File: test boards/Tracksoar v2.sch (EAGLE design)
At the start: 37 parts, among them IC1 BME280, IC2 74AHC1G125DBV, Y1 16MHZ

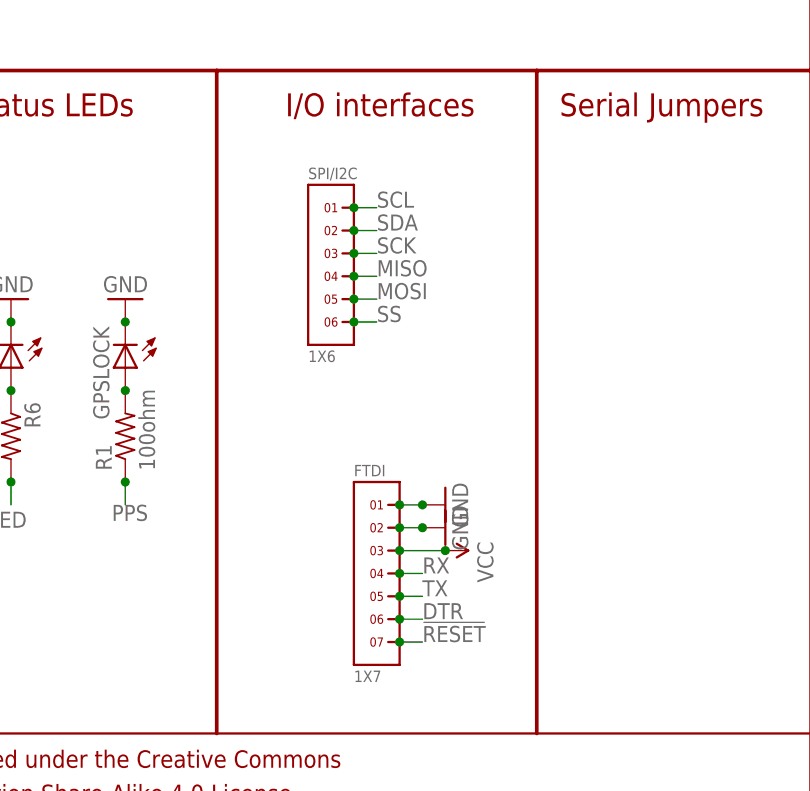
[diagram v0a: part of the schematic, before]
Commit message: Removed v1.1 headers
removed the v1.1 headers to simplify layout.
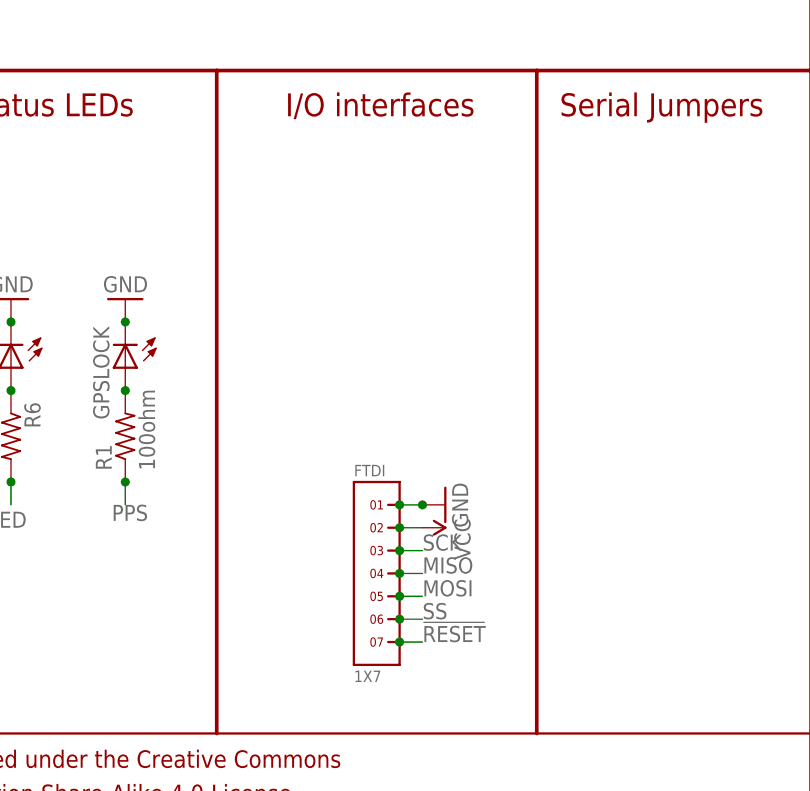
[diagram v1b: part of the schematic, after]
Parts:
- removed SPI/I2C: 1X6, headers(2mm):1X6
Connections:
- removed net DTR: FTDI.6
- net GND: no longer FTDI.2
- net MISO: now also FTDI.4; no longer SPI/I2C.4
- net MOSI: now also FTDI.5; no longer SPI/I2C.5
- net RX: no longer FTDI.4
- net SCK: now also FTDI.3; no longer SPI/I2C.3
- net SCL: no longer SPI/I2C.1
- net SDA: no longer SPI/I2C.2
- net SS: now also FTDI.6; no longer SPI/I2C.6
- net TX: no longer FTDI.5
- net VCC: now also FTDI.2; no longer FTDI.3
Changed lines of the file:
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@@
 <part name="GND1" library="SparkFun-Aesthetics" deviceset="GND" device=""/>
 <part name="GND3" library="SparkFun-Aesthetics" deviceset="GND" device=""/>
-<part name="GND10" library="SparkFun-Aesthetics" deviceset="GND" device=""/>
 <part name="GND20" library="SparkFun-Aesthetics" deviceset="GND" device=""/>
 <part name="R3" library="adafruit" deviceset="R-US_" device="R0402" value="4.7k"/>
@@
 <part name="GPS-ANT" library="SparkFun-RF" deviceset="ANTENNA2" device="SMD3"/>
 <part name="FTDI" library="headers(2mm)" deviceset="1X7" device=""/>
-<part name="SPI/I2C" library="headers(2mm)" deviceset="1X6" device=""/>
 <part name="GND5" library="SparkFun-Aesthetics" deviceset="GND" device=""/>
 <part name="IC1" library="bosch-bme280" deviceset="BME280" device=""/>
@@
 <instance part="GND21" gate="1" x="22.86" y="12.7" rot="R270"/>
 <instance part="GND22" gate="1" x="208.28" y="60.96" rot="R90"/>
-<instance part="SUPPLY9" gate="G$1" x="208.28" y="55.88" rot="R270"/>
+<instance part="SUPPLY9" gate="G$1" x="205.74" y="58.42" rot="R270"/>
 <instance part="R5" gate="G$1" x="25.4" y="73.66" rot="R90"/>
 <instance part="SUPPLY10" gate="G$1" x="25.4" y="78.74"/>
@@
 <instance part="GND1" gate="1" x="66.04" y="167.64" rot="R90"/>
 <instance part="GND3" gate="1" x="17.78" y="157.48"/>
-<instance part="GND10" gate="1" x="208.28" y="58.42" rot="R90"/>
 <instance part="GND20" gate="1" x="106.68" y="76.2" rot="R270"/>
 <instance part="R3" gate="G$1" x="129.54" y="48.26" rot="R270"/>
@@
 <instance part="GPS-ANT" gate="G$1" x="165.1" y="165.1" rot="R90"/>
 <instance part="FTDI" gate="G$1" x="200.66" y="53.34"/>
-<instance part="SPI/I2C" gate="G$1" x="195.58" y="86.36"/>
 <instance part="GND5" gate="1" x="38.1" y="167.64"/>
 <instance part="IC1" gate="G$1" x="121.92" y="81.28"/>
@@
 </segment>
 <segment>
-<wire x1="203.2" y1="58.42" x2="205.74" y2="58.42" width="0.1524" layer="91"/>
-<pinref part="GND10" gate="1" pin="GND"/>
-<junction x="205.74" y="58.42"/>
-<pinref part="FTDI" gate="G$1" pin="2"/>
-<junction x="203.2" y="58.42"/>
-</segment>
-<segment>
 <pinref part="LT3426" gate="G$1" pin="GND"/>
 <pinref part="GND27" gate="1" pin="GND"/>
@@
 <junction x="53.34" y="152.4"/>
 <wire x1="55.88" y1="152.4" x2="53.34" y2="152.4" width="0.1524" layer="91"/>
-</segment>
-<segment>
-<wire x1="203.2" y1="55.88" x2="208.28" y2="55.88" width="0.1524" layer="91"/>
-<pinref part="SUPPLY9" gate="G$1" pin="VCC"/>
-<junction x="208.28" y="55.88"/>
-<pinref part="FTDI" gate="G$1" pin="3"/>
-<junction x="203.2" y="55.88"/>
 </segment>
 <segment>
@@
 <junction x="40.64" y="99.06"/>
 </segment>
+<segment>
+<pinref part="FTDI" gate="G$1" pin="2"/>
+<pinref part="SUPPLY9" gate="G$1" pin="VCC"/>
+<wire x1="205.74" y1="58.42" x2="203.2" y2="58.42" width="0.1524" layer="91"/>
+<junction x="203.2" y="58.42"/>
+</segment>
 </net>
 <net name="3V" class="0">
@@
 </segment>
 </net>
-<net name="DTR" class="0">
-<segment>
-<wire x1="203.2" y1="48.26" x2="205.74" y2="48.26" width="0.1524" layer="91"/>
+<net name="RXO" class="0">
+<segment>
+<wire x1="73.66" y1="45.72" x2="76.2" y2="45.72" width="0.1524" layer="91"/>
+<label x="76.2" y="45.72" size="1.778" layer="95"/>
+</segment>
+</net>
+<net name="TXO" class="0">
+<segment>
+<wire x1="73.66" y1="43.18" x2="76.2" y2="43.18" width="0.1524" layer="91"/>
+<label x="76.2" y="43.18" size="1.778" layer="95"/>
+</segment>
+</net>
+<net name="MISO" class="0">
+<segment>
+<wire x1="73.66" y1="12.7" x2="76.2" y2="12.7" width="0.1524" layer="91"/>
+<label x="76.2" y="12.7" size="1.778" layer="95"/>
+</segment>
+<segment>
+<wire x1="-25.4" y1="12.7" x2="-22.86" y2="12.7" width="0.1524" layer="91"/>
+<pinref part="U$4" gate="G$1" pin="PB3(MISO)"/>
+<junction x="-25.4" y="12.7"/>
+</segment>
+<segment>
+<wire x1="205.74" y1="53.34" x2="203.2" y2="53.34" width="0.1524" layer="91"/>
+<label x="205.74" y="53.34" size="1.778" layer="95"/>
+<pinref part="FTDI" gate="G$1" pin="4"/>
+<junction x="203.2" y="53.34"/>
+</segment>
+</net>
+<net name="MOSI" class="0">
+<segment>
+<wire x1="73.66" y1="15.24" x2="76.2" y2="15.24" width="0.1524" layer="91"/>
+<label x="76.2" y="15.24" size="1.778" layer="95"/>
+</segment>
+<segment>
+<wire x1="-25.4" y1="15.24" x2="-22.86" y2="15.24" width="0.1524" layer="91"/>
+<pinref part="U$4" gate="G$1" pin="PB2(MOSI)"/>
+<junction x="-25.4" y="15.24"/>
+</segment>
+<segment>
+<wire x1="205.74" y1="50.8" x2="203.2" y2="50.8" width="0.1524" layer="91"/>
+<label x="205.74" y="50.8" size="1.778" layer="95"/>
+<pinref part="FTDI" gate="G$1" pin="5"/>
+<junction x="203.2" y="50.8"/>
+</segment>
+</net>
+<net name="SCK" class="0">
+<segment>
+<wire x1="73.66" y1="10.16" x2="76.2" y2="10.16" width="0.1524" layer="91"/>
+<label x="76.2" y="10.16" size="1.778" layer="95"/>
+</segment>
+<segment>
+<wire x1="-25.4" y1="17.78" x2="-22.86" y2="17.78" width="0.1524" layer="91"/>
+<pinref part="U$4" gate="G$1" pin="PB1(SCK)"/>
+<junction x="-25.4" y="17.78"/>
+</segment>
+<segment>
+<wire x1="205.74" y1="55.88" x2="203.2" y2="55.88" width="0.1524" layer="91"/>
+<label x="205.74" y="55.88" size="1.778" layer="95"/>
+<pinref part="FTDI" gate="G$1" pin="3"/>
+<junction x="203.2" y="55.88"/>
+</segment>
+</net>
+<net name="SS" class="0">
+<segment>
+<wire x1="73.66" y1="17.78" x2="76.2" y2="17.78" width="0.1524" layer="91"/>
+<label x="76.2" y="17.78" size="1.778" layer="95"/>
+</segment>
+<segment>
+<wire x1="-25.4" y1="20.32" x2="-22.86" y2="20.32" width="0.1524" layer="91"/>
+<pinref part="U$4" gate="G$1" pin="PB0(SS)"/>
+<junction x="-25.4" y="20.32"/>
+</segment>
+<segment>
+<wire x1="205.74" y1="48.26" x2="203.2" y2="48.26" width="0.1524" layer="91"/>
 <label x="205.74" y="48.26" size="1.778" layer="95"/>
 <pinref part="FTDI" gate="G$1" pin="6"/>
 <junction x="203.2" y="48.26"/>
-</segment>
-</net>
-<net name="RXO" class="0">
-<segment>
-<wire x1="73.66" y1="45.72" x2="76.2" y2="45.72" width="0.1524" layer="91"/>
-<label x="76.2" y="45.72" size="1.778" layer="95"/>
-</segment>
-</net>
-<net name="TXO" class="0">
-<segment>
-<wire x1="73.66" y1="43.18" x2="76.2" y2="43.18" width="0.1524" layer="91"/>
-<label x="76.2" y="43.18" size="1.778" layer="95"/>
-</segment>
-</net>
-<net name="MISO" class="0">
-<segment>
-<wire x1="73.66" y1="12.7" x2="76.2" y2="12.7" width="0.1524" layer="91"/>
-<label x="76.2" y="12.7" size="1.778" layer="95"/>
-</segment>
-<segment>
-<wire x1="200.66" y1="86.36" x2="198.12" y2="86.36" width="0.1524" layer="91"/>
-<label x="200.66" y="86.36" size="1.778" layer="95"/>
-<pinref part="SPI/I2C" gate="G$1" pin="4"/>
-<junction x="198.12" y="86.36"/>
-</segment>
-<segment>
-<wire x1="-25.4" y1="12.7" x2="-22.86" y2="12.7" width="0.1524" layer="91"/>
-<pinref part="U$4" gate="G$1" pin="PB3(MISO)"/>
-<junction x="-25.4" y="12.7"/>
-</segment>
-</net>
-<net name="MOSI" class="0">
-<segment>
-<wire x1="73.66" y1="15.24" x2="76.2" y2="15.24" width="0.1524" layer="91"/>
-<label x="76.2" y="15.24" size="1.778" layer="95"/>
-</segment>
-<segment>
-<wire x1="200.66" y1="83.82" x2="198.12" y2="83.82" width="0.1524" layer="91"/>
-<label x="200.66" y="83.82" size="1.778" layer="95"/>
-<pinref part="SPI/I2C" gate="G$1" pin="5"/>
-<junction x="198.12" y="83.82"/>
-</segment>
-<segment>
-<wire x1="-25.4" y1="15.24" x2="-22.86" y2="15.24" width="0.1524" layer="91"/>
-<pinref part="U$4" gate="G$1" pin="PB2(MOSI)"/>
-<junction x="-25.4" y="15.24"/>
-</segment>
-</net>
-<net name="SCK" class="0">
-<segment>
-<wire x1="73.66" y1="10.16" x2="76.2" y2="10.16" width="0.1524" layer="91"/>
-<label x="76.2" y="10.16" size="1.778" layer="95"/>
-</segment>
-<segment>
-<wire x1="200.66" y1="88.9" x2="198.12" y2="88.9" width="0.1524" layer="91"/>
-<label x="200.66" y="88.9" size="1.778" layer="95"/>
-<pinref part="SPI/I2C" gate="G$1" pin="3"/>
-<junction x="198.12" y="88.9"/>
-</segment>
-<segment>
-<wire x1="-25.4" y1="17.78" x2="-22.86" y2="17.78" width="0.1524" layer="91"/>
-<pinref part="U$4" gate="G$1" pin="PB1(SCK)"/>
-<junction x="-25.4" y="17.78"/>
-</segment>
-</net>
-<net name="SS" class="0">
-<segment>
-<wire x1="73.66" y1="17.78" x2="76.2" y2="17.78" width="0.1524" layer="91"/>
-<label x="76.2" y="17.78" size="1.778" layer="95"/>
-</segment>
-<segment>
-<wire x1="200.66" y1="81.28" x2="198.12" y2="81.28" width="0.1524" layer="91"/>
-<label x="200.66" y="81.28" size="1.778" layer="95"/>
-<pinref part="SPI/I2C" gate="G$1" pin="6"/>
-<junction x="198.12" y="81.28"/>
-</segment>
-<segment>
-<wire x1="-25.4" y1="20.32" x2="-22.86" y2="20.32" width="0.1524" layer="91"/>
-<pinref part="U$4" gate="G$1" pin="PB0(SS)"/>
-<junction x="-25.4" y="20.32"/>
 </segment>
 </net>
@@
 </segment>
 <segment>
-<wire x1="200.66" y1="91.44" x2="198.12" y2="91.44" width="0.1524" layer="91"/>
-<label x="200.66" y="91.44" size="1.778" layer="95"/>
-<pinref part="SPI/I2C" gate="G$1" pin="2"/>
-<junction x="198.12" y="91.44"/>
-</segment>
-<segment>
 <wire x1="-25.4" y1="50.8" x2="-22.86" y2="50.8" width="0.1524" layer="91"/>
 <pinref part="U$4" gate="G$1" pin="PD1(SDA)"/>
@@
 <label x="137.16" y="40.64" size="1.778" layer="95"/>
 <junction x="137.16" y="43.18"/>
-</segment>
-<segment>
-<wire x1="200.66" y1="93.98" x2="198.12" y2="93.98" width="0.1524" layer="91"/>
-<label x="200.66" y="93.98" size="1.778" layer="95"/>
-<pinref part="SPI/I2C" gate="G$1" pin="1"/>
-<junction x="198.12" y="93.98"/>
 </segment>
 <segment>
@@
 <junction x="106.68" y="7.62"/>
 </segment>
-<segment>
-<wire x1="203.2" y1="50.8" x2="205.74" y2="50.8" width="0.1524" layer="91"/>
-<label x="205.74" y="50.8" size="1.778" layer="95"/>
-<pinref part="FTDI" gate="G$1" pin="5"/>
-<junction x="203.2" y="50.8"/>
-</segment>
 </net>
 <net name="RX" class="0">
@@
 </segment>
 <segment>
-<wire x1="203.2" y1="53.34" x2="205.74" y2="53.34" width="0.1524" layer="91"/>
-<label x="205.74" y="53.34" size="1.778" layer="95"/>
-<pinref part="FTDI" gate="G$1" pin="4"/>
-<junction x="203.2" y="53.34"/>
-</segment>
-<segment>

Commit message: Tracksoar v2 rev2
finalized routing, added 3v access to programming header
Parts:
- FTDI: value 1X7 -> 1X8; device headers(2mm):1X7 -> headers(2mm):1X8
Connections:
- net 3V: now also FTDI.1
- net GND: now also FTDI.8; no longer FTDI.1
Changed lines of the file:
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@@
 <part name="GND30" library="SparkFun-Aesthetics" deviceset="GND" device=""/>
 <part name="GPS-ANT" library="SparkFun-RF" deviceset="ANTENNA2" device="SMD3"/>
-<part name="FTDI" library="headers(2mm)" deviceset="1X7" device=""/>
+<part name="FTDI" library="headers(2mm)" deviceset="1X8" device=""/>
 <part name="GND5" library="SparkFun-Aesthetics" deviceset="GND" device=""/>
 <part name="IC1" library="bosch-bme280" deviceset="BME280" device=""/>
@@
 <instance part="GND12" gate="1" x="22.86" y="15.24" rot="R270"/>
 <instance part="GND21" gate="1" x="22.86" y="12.7" rot="R270"/>
-<instance part="GND22" gate="1" x="208.28" y="60.96" rot="R90"/>
+<instance part="GND22" gate="1" x="208.28" y="43.18" rot="R90"/>
 <instance part="SUPPLY9" gate="G$1" x="205.74" y="58.42" rot="R270"/>
 <instance part="R5" gate="G$1" x="25.4" y="73.66" rot="R90"/>
@@
 <instance part="GND30" gate="1" x="53.34" y="127"/>
 <instance part="GPS-ANT" gate="G$1" x="165.1" y="165.1" rot="R90"/>
-<instance part="FTDI" gate="G$1" x="200.66" y="53.34"/>
+<instance part="FTDI" gate="G$1" x="200.66" y="50.8"/>
 <instance part="GND5" gate="1" x="38.1" y="167.64"/>
 <instance part="IC1" gate="G$1" x="121.92" y="81.28"/>
@@
 </segment>
 <segment>
-<wire x1="203.2" y1="60.96" x2="205.74" y2="60.96" width="0.1524" layer="91"/>
-<pinref part="GND22" gate="1" pin="GND"/>
-<junction x="205.74" y="60.96"/>
-<pinref part="FTDI" gate="G$1" pin="1"/>
-<junction x="203.2" y="60.96"/>
-</segment>
-<segment>
 <pinref part="PTT" gate="G$1" pin="C"/>
 <pinref part="GND26" gate="1" pin="GND"/>
@@
 <junction x="27.94" y="101.6"/>
 <junction x="38.1" y="101.6"/>
+</segment>
+<segment>
+<pinref part="FTDI" gate="G$1" pin="8"/>
+<pinref part="GND22" gate="1" pin="GND"/>
+<wire x1="205.74" y1="43.18" x2="203.2" y2="43.18" width="0.1524" layer="91"/>
+<junction x="203.2" y="43.18"/>
 </segment>
 </net>
@@
 <junction x="99.06" y="81.28"/>
 </segment>
+<segment>
+<pinref part="FTDI" gate="G$1" pin="1"/>
+<wire x1="203.2" y1="60.96" x2="205.74" y2="60.96" width="0.1524" layer="91"/>
+<junction x="203.2" y="60.96"/>
+</segment>
 </net>
